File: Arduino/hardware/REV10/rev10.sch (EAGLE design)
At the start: 43 parts, among them IC2 ATMEGA168-AU, Q1 32768Hz, Q2 BSS84, U1 TC1185SMD, U2 ARDUINOR3-DIMENSION

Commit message: updates to rev10
fully routed
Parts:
- LED, LED1: device adafruit:LED3MM -> led:LEDCHIP-LED0603
- U2: value ARDUINOR3-DIMENSION -> ARDUINO; device adafruit:ARDUINOR3-DIMENSION -> arduino:ARDUINO
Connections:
- net 5VGSM: now also U2.5V
- net N$11: now also U2.D9
- net N$19: now also U2.D7
- net N$20: now also U2.D8
- net PFET: now also IC2.ANALOG_3
- net RESET: now also U2./RESET
- net VCC: now also U2.3V
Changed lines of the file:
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@@
 <part name="C12" library="resistor" deviceset="C-EU" device="C0603" value="100nF"/>
 <part name="R10" library="resistor" deviceset="R-EU_" device="R0603" value="1K"/>
-<part name="LED" library="adafruit" deviceset="LED" device="3MM"/>
+<part name="LED" library="led" deviceset="LED" device="CHIP-LED0603"/>
 <part name="P+7" library="SparkFun-Aesthetics" deviceset="VCC" device=""/>
 <part name="RFM23B" library="SparkFun-RF" deviceset="RFM23B" device=""/>
@@
 <part name="P+8" library="SparkFun-Aesthetics" deviceset="VCC" device=""/>
 <part name="GND8" library="SparkFun-Aesthetics" deviceset="GND" device=""/>
-<part name="U2" library="adafruit" deviceset="ARDUINOR3" device="-DIMENSION"/>
+<part name="U2" library="arduino" deviceset="ARDUINO" device=""/>
 <part name="GND1" library="SparkFun-Aesthetics" deviceset="GND" device=""/>
 <part name="X1" library="con-wago-500" deviceset="W237-102" device=""/>
@@
 <part name="GND9" library="SparkFun-Aesthetics" deviceset="GND" device=""/>
 <part name="R11" library="resistor" deviceset="R-EU_" device="R0603" value="470R"/>
-<part name="LED1" library="adafruit" deviceset="LED" device="3MM"/>
+<part name="LED1" library="led" deviceset="LED" device="CHIP-LED0603"/>
 <part name="T1" library="transistor" deviceset="*-NPN-" device="SOT23-EBC"/>
 <part name="R13" library="resistor" deviceset="R-EU_" device="R0603" value="1K"/>
@@
 <instance part="P+8" gate="1" x="256.54" y="246.38"/>
 <instance part="GND8" gate="1" x="251.46" y="223.52"/>
-<instance part="U2" gate="G$1" x="198.12" y="160.02" rot="R90"/>
+<instance part="U2" gate="G$1" x="223.52" y="127" rot="R90"/>
 <instance part="GND1" gate="1" x="63.5" y="177.8"/>
 <instance part="X1" gate="-1" x="20.32" y="190.5"/>
@@
 <wire x1="228.6" y1="154.94" x2="233.68" y2="154.94" width="0.1524" layer="91"/>
 <label x="233.68" y="154.94" size="1.778" layer="95"/>
+<pinref part="U2" gate="G$1" pin="3V"/>
 </segment>
 <segment>
@@
 <wire x1="226.06" y1="106.68" x2="203.2" y2="106.68" width="0.1524" layer="91"/>
 <wire x1="203.2" y1="106.68" x2="203.2" y2="182.88" width="0.1524" layer="91"/>
+<wire x1="203.2" y1="182.88" x2="228.6" y2="182.88" width="0.1524" layer="91"/>
 <pinref part="U2" gate="G$1" pin="A5/SCL"/>
-<wire x1="203.2" y1="182.88" x2="228.6" y2="182.88" width="0.1524" layer="91"/>
 <pinref part="IC2" gate="1" pin="ANALOG_5"/>
 <junction x="226.06" y="106.68"/>
@@
 <wire x1="236.22" y1="152.4" x2="228.6" y2="152.4" width="0.1524" layer="91"/>
 <label x="238.76" y="152.4" size="1.778" layer="95"/>
+<pinref part="U2" gate="G$1" pin="/RESET"/>
 </segment>
 </net>
@@
 <wire x1="248.92" y1="111.76" x2="226.06" y2="111.76" width="0.1524" layer="91"/>
 <label x="251.46" y="111.76" size="1.778" layer="95"/>
+<pinref part="IC2" gate="1" pin="ANALOG_3"/>
 </segment>
 <segment>
@@
 <wire x1="185.42" y1="157.48" x2="167.64" y2="157.48" width="0.1524" layer="91"/>
 <pinref part="IC2" gate="1" pin="DIGITAL_5(PWM)"/>
+<pinref part="U2" gate="G$1" pin="D8"/>
 </segment>
 </net>
@@
 <pinref part="R5" gate="G$1" pin="2"/>
 <wire x1="195.58" y1="73.66" x2="190.5" y2="73.66" width="0.1524" layer="91"/>
+<pinref part="U2" gate="G$1" pin="D7"/>
 </segment>
 </net>
@@
 <wire x1="317.5" y1="43.18" x2="317.5" y2="114.3" width="0.1524" layer="91"/>
 <wire x1="317.5" y1="114.3" x2="226.06" y2="114.3" width="0.1524" layer="91"/>
+<pinref part="U2" gate="G$1" pin="D9"/>
 </segment>
 </net>
@@
 <wire x1="228.6" y1="157.48" x2="236.22" y2="157.48" width="0.1524" layer="91"/>
 <label x="231.14" y="157.48" size="1.778" layer="95"/>
-</segment>
-</net>
+<pinref part="U2" gate="G$1" pin="5V"/>
+</segment>
+</net>

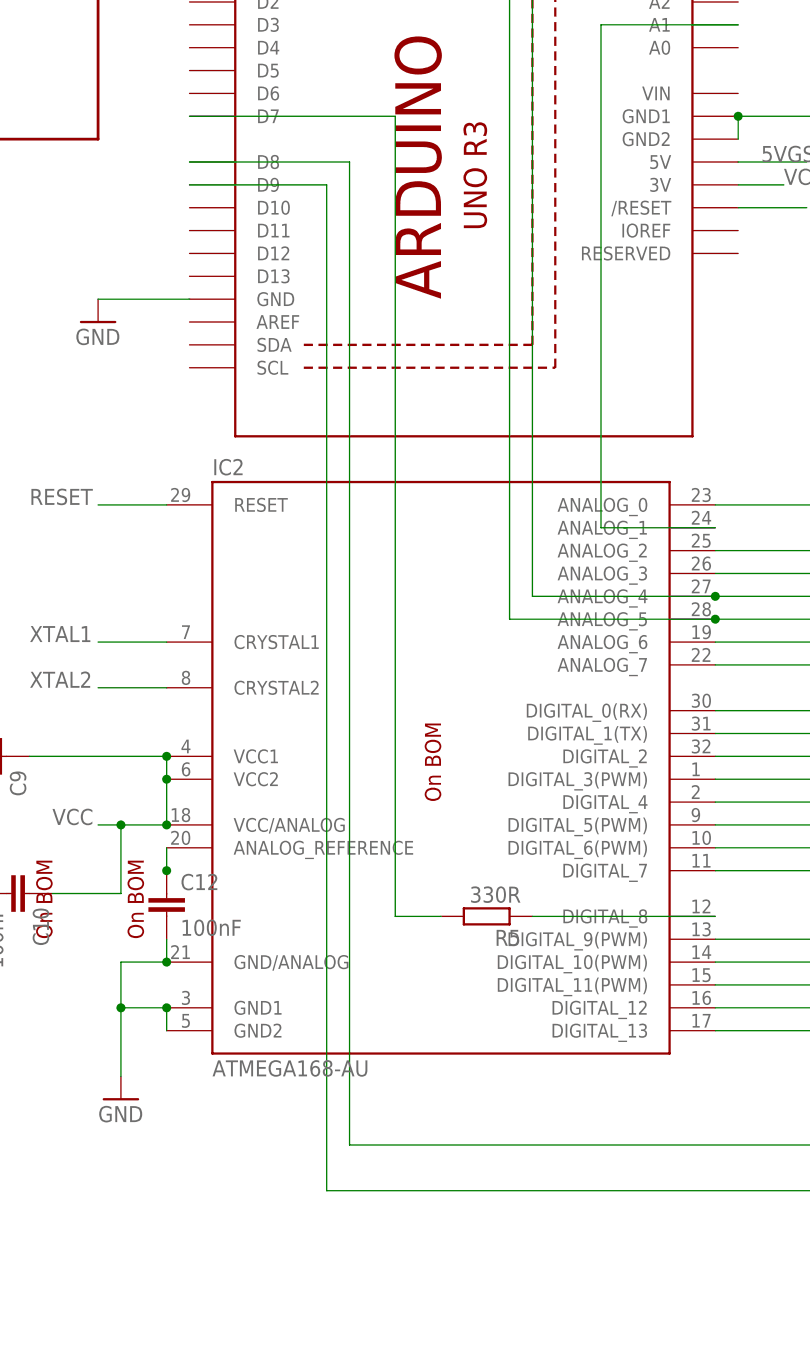
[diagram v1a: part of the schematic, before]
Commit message: added 2 missing resistors on rev10
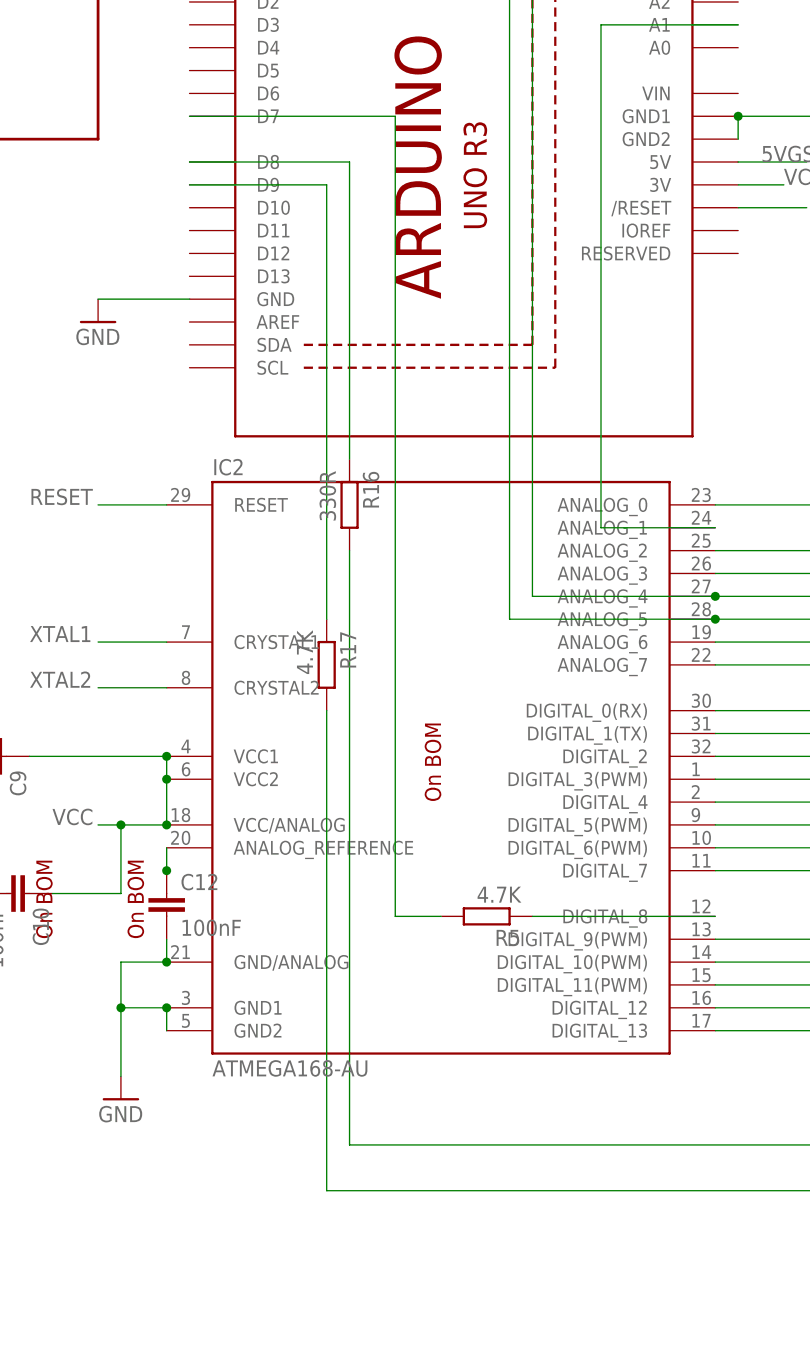
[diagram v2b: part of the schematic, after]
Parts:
- added R16: 330R, resistor:R-EU_R0603
- added R17: 4.7K, resistor:R-EU_R0603
- R5: value 330R -> 4.7K
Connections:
- new net N$30: R17.1, U2.D9
- new net N$32: R16.1, U2.D8
- net N$11: no longer U2.D9
- net N$20: now also R16.2; no longer U2.D8
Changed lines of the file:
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@@
 <part name="I2C_EXT" library="pinhead" deviceset="PINHD-2X7" device="/90"/>
 <part name="IC2" library="Arduino-AVR" deviceset="ATMEGA168" device="-AU"/>
-<part name="R5" library="resistor" deviceset="R-EU_" device="R0603" value="330R"/>
 <part name="USBPOWER" library="micro-usb-fci-10103592" deviceset="MICRO-USB-FCI-10103592" device=""/>
 <part name="GND14" library="SparkFun-Aesthetics" deviceset="GND" device=""/>
@@
 <part name="REL1" library="OJE-SS-103HM" deviceset="OJE-SS-103HM" device=""/>
 <part name="X3" library="con-wago-500" deviceset="W237-102" device=""/>
+<part name="R16" library="resistor" deviceset="R-EU_" device="R0603" value="330R"/>
+<part name="R5" library="resistor" deviceset="R-EU_" device="R0603" value="4.7K"/>
+<part name="R17" library="resistor" deviceset="R-EU_" device="R0603" value="4.7K"/>
 </parts>
 <sheets>
@@
 <instance part="I2C_EXT" gate="A" x="124.46" y="213.36" rot="R90"/>
 <instance part="IC2" gate="1" x="195.58" y="91.44"/>
-<instance part="R5" gate="G$1" x="200.66" y="73.66" rot="R180"/>
 <instance part="USBPOWER" gate="G$1" x="12.7" y="243.84" rot="R270"/>
 <instance part="GND14" gate="1" x="15.24" y="214.63"/>
@@
 <instance part="X3" gate="-1" x="342.9" y="96.52"/>
 <instance part="X3" gate="-2" x="342.9" y="91.44"/>
+<instance part="R16" gate="G$1" x="185.42" y="119.38" rot="R270"/>
+<instance part="R5" gate="G$1" x="200.66" y="73.66" rot="R180"/>
+<instance part="R17" gate="G$1" x="182.88" y="101.6" rot="R270"/>
 </instances>
 <busses>
@@
 <wire x1="276.86" y1="83.82" x2="276.86" y2="48.26" width="0.1524" layer="91"/>
 <wire x1="276.86" y1="48.26" x2="185.42" y2="48.26" width="0.1524" layer="91"/>
-<wire x1="185.42" y1="48.26" x2="185.42" y2="157.48" width="0.1524" layer="91"/>
-<wire x1="185.42" y1="157.48" x2="167.64" y2="157.48" width="0.1524" layer="91"/>
+<wire x1="185.42" y1="48.26" x2="185.42" y2="114.3" width="0.1524" layer="91"/>
 <pinref part="IC2" gate="1" pin="DIGITAL_5(PWM)"/>
-<pinref part="U2" gate="G$1" pin="D8"/>
+<pinref part="R16" gate="G$1" pin="2"/>
 </segment>
 </net>
@@
 <wire x1="190.5" y1="73.66" x2="190.5" y2="162.56" width="0.1524" layer="91"/>
 <wire x1="190.5" y1="162.56" x2="167.64" y2="162.56" width="0.1524" layer="91"/>
-<pinref part="R5" gate="G$1" pin="2"/>
 <wire x1="195.58" y1="73.66" x2="190.5" y2="73.66" width="0.1524" layer="91"/>
 <pinref part="U2" gate="G$1" pin="D7"/>
+<pinref part="R5" gate="G$1" pin="2"/>
 </segment>
 </net>
@@
 <net name="N$3" class="0">
 <segment>
-<pinref part="R5" gate="G$1" pin="1"/>
 <pinref part="IC2" gate="1" pin="DIGITAL_8"/>
 <wire x1="205.74" y1="73.66" x2="226.06" y2="73.66" width="0.1524" layer="91"/>
+<pinref part="R5" gate="G$1" pin="1"/>
 </segment>
 </net>
@@
 <segment>
 <pinref part="IC2" gate="1" pin="ANALOG_2"/>
-<wire x1="167.64" y1="154.94" x2="182.88" y2="154.94" width="0.1524" layer="91"/>
-<wire x1="182.88" y1="154.94" x2="182.88" y2="43.18" width="0.1524" layer="91"/>
+<wire x1="182.88" y1="96.52" x2="182.88" y2="43.18" width="0.1524" layer="91"/>
 <wire x1="182.88" y1="43.18" x2="317.5" y2="43.18" width="0.1524" layer="91"/>
 <wire x1="317.5" y1="43.18" x2="317.5" y2="114.3" width="0.1524" layer="91"/>
 <wire x1="317.5" y1="114.3" x2="226.06" y2="114.3" width="0.1524" layer="91"/>
-<pinref part="U2" gate="G$1" pin="D9"/>
 </segment>
 </net>
@@
 </segment>
 </net>
+<net name="N$30" class="0">
+<segment>
+<pinref part="U2" gate="G$1" pin="D9"/>
+<wire x1="167.64" y1="154.94" x2="182.88" y2="154.94" width="0.1524" layer="91"/>
+<wire x1="182.88" y1="154.94" x2="182.88" y2="106.68" width="0.1524" layer="91"/>
+<pinref part="R17" gate="G$1" pin="1"/>
+</segment>
+</net>
+<net name="N$32" class="0">
+<segment>
+<pinref part="U2" gate="G$1" pin="D8"/>
+<wire x1="185.42" y1="157.48" x2="167.64" y2="157.48" width="0.1524" layer="91"/>
+<pinref part="R16" gate="G$1" pin="1"/>
+<wire x1="185.42" y1="124.46" x2="185.42" y2="157.48" width="0.1524" layer="91"/>
+</segment>
+</net>

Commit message: routed rev10 again
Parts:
- renumbered Q2 to PFET
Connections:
- net N$11: now also R17.2
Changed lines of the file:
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@@
 <part name="GND10" library="SparkFun-Aesthetics" deviceset="GND" device=""/>
 <part name="JP2" library="pinhead" deviceset="PINHD-2X3" device="/90"/>
-<part name="Q2" library="transistor-small-signal" deviceset="BSS84" device=""/>
+<part name="PFET" library="transistor-small-signal" deviceset="BSS84" device=""/>
 <part name="R15" library="resistor" deviceset="R-EU_" device="R0603" value="4.7K"/>
 <part name="REL1" library="OJE-SS-103HM" deviceset="OJE-SS-103HM" device=""/>
@@
 <text x="152.4" y="71.12" size="1.778" layer="94" rot="R90">On BOM</text>
 <text x="162.56" y="71.12" size="1.778" layer="94" rot="R90">On BOM</text>
-<text x="195.58" y="86.36" size="1.778" layer="94" rot="R90">On BOM</text>
+<text x="190.5" y="114.3" size="1.778" layer="94" rot="R90">On BOM</text>
 <text x="307.34" y="177.8" size="1.778" layer="94" rot="R90">On BOM</text>
 <text x="45.72" y="175.26" size="1.778" layer="94" rot="R180">On BOM</text>
@@
 <wire x1="281.94" y1="157.48" x2="281.94" y2="124.46" width="0.3048" layer="94"/>
 <wire x1="281.94" y1="124.46" x2="325.12" y2="124.46" width="0.3048" layer="94"/>
+<text x="180.34" y="96.52" size="1.778" layer="94" rot="R90">On BOM</text>
+<text x="203.2" y="78.74" size="1.778" layer="94" rot="R180">On BOM</text>
+<text x="297.18" y="139.7" size="1.778" layer="94">On BOM</text>
+<text x="355.6" y="142.24" size="1.778" layer="94">On BOM</text>
+<text x="347.98" y="129.54" size="1.778" layer="94" rot="R90">On BOM</text>
+<text x="360.68" y="124.46" size="1.778" layer="94" rot="R90">On BOM</text>
+<text x="358.14" y="96.52" size="1.778" layer="94" rot="R90">On BOM</text>
+<text x="345.44" y="129.54" size="1.778" layer="94" rot="R180">On BOM</text>
+<text x="353.06" y="119.38" size="1.778" layer="94" rot="R180">On BOM</text>
+<text x="15.24" y="193.04" size="1.778" layer="94" rot="R270">On BOM</text>
+<text x="332.74" y="96.52" size="1.778" layer="94" rot="R270">On BOM</text>
+<text x="279.4" y="109.22" size="1.778" layer="94" rot="R270">On BOM</text>
 </plain>
 <instances>
@@
 <instance part="GND10" gate="1" x="335.28" y="124.46" rot="R270"/>
 <instance part="JP2" gate="A" x="276.86" y="106.68"/>
-<instance part="Q2" gate="G$1" x="314.96" y="142.24"/>
+<instance part="PFET" gate="G$1" x="314.96" y="142.24" smashed="yes">
+<attribute name="NAME" x="317.5" y="142.24" size="1.778" layer="95"/>
+</instance>
 <instance part="R15" gate="G$1" x="302.26" y="144.78" smashed="yes" rot="R180">
 <attribute name="NAME" x="300.99" y="148.3614" size="1.778" layer="95" rot="R180"/>
@@
 <wire x1="314.96" y1="147.32" x2="314.96" y2="152.4" width="0.1524" layer="91"/>
 <label x="309.88" y="152.4" size="1.778" layer="95"/>
-<pinref part="Q2" gate="G$1" pin="S"/>
+<pinref part="PFET" gate="G$1" pin="S"/>
 </segment>
 </net>
@@
 <wire x1="317.5" y1="43.18" x2="317.5" y2="114.3" width="0.1524" layer="91"/>
 <wire x1="317.5" y1="114.3" x2="226.06" y2="114.3" width="0.1524" layer="91"/>
+<pinref part="R17" gate="G$1" pin="2"/>
 </segment>
 </net>
@@
 <segment>
 <pinref part="R15" gate="G$1" pin="1"/>
-<pinref part="Q2" gate="G$1" pin="G"/>
+<pinref part="PFET" gate="G$1" pin="G"/>
 <wire x1="307.34" y1="144.78" x2="309.88" y2="144.78" width="0.1524" layer="91"/>
 </segment>
@@
 <net name="5VGSM" class="0">
 <segment>
-<pinref part="Q2" gate="G$1" pin="D"/>
+<pinref part="PFET" gate="G$1" pin="D"/>
 <wire x1="314.96" y1="137.16" x2="314.96" y2="129.54" width="0.1524" layer="91"/>
 <label x="304.8" y="129.54" size="1.778" layer="95"/>

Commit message: updates to rev 10
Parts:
- added DQ/D2: (no value), wirepad:2,15/1,0
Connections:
- net D2: now also DQ/D2.P
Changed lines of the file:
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@@
 <part name="R5" library="resistor" deviceset="R-EU_" device="R0603" value="4.7K"/>
 <part name="R17" library="resistor" deviceset="R-EU_" device="R0603" value="4.7K"/>
+<part name="DQ/D2" library="wirepad" deviceset="2,15/1,0" device=""/>
 </parts>
 <sheets>
@@
 <instance part="R5" gate="G$1" x="200.66" y="73.66" rot="R180"/>
 <instance part="R17" gate="G$1" x="182.88" y="101.6" rot="R270"/>
+<instance part="DQ/D2" gate="1" x="134.62" y="223.52" rot="R180"/>
 </instances>
 <busses>
@@
 <net name="D2" class="0">
 <segment>
-<wire x1="132.08" y1="231.14" x2="132.08" y2="218.44" width="0.1524" layer="91"/>
+<wire x1="132.08" y1="231.14" x2="132.08" y2="223.52" width="0.1524" layer="91"/>
 <label x="134.62" y="231.14" size="1.778" layer="95"/>
 <pinref part="I2C_EXT" gate="A" pin="14"/>
-</segment>
-<segment>
+<pinref part="DQ/D2" gate="1" pin="P"/>
+<wire x1="132.08" y1="223.52" x2="132.08" y2="218.44" width="0.1524" layer="91"/>
+<junction x="132.08" y="223.52"/>
+</segment>
+<segment>
